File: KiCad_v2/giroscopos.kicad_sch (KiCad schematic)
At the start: 15 parts, among them U8 BNO085, U9 MPU-6050

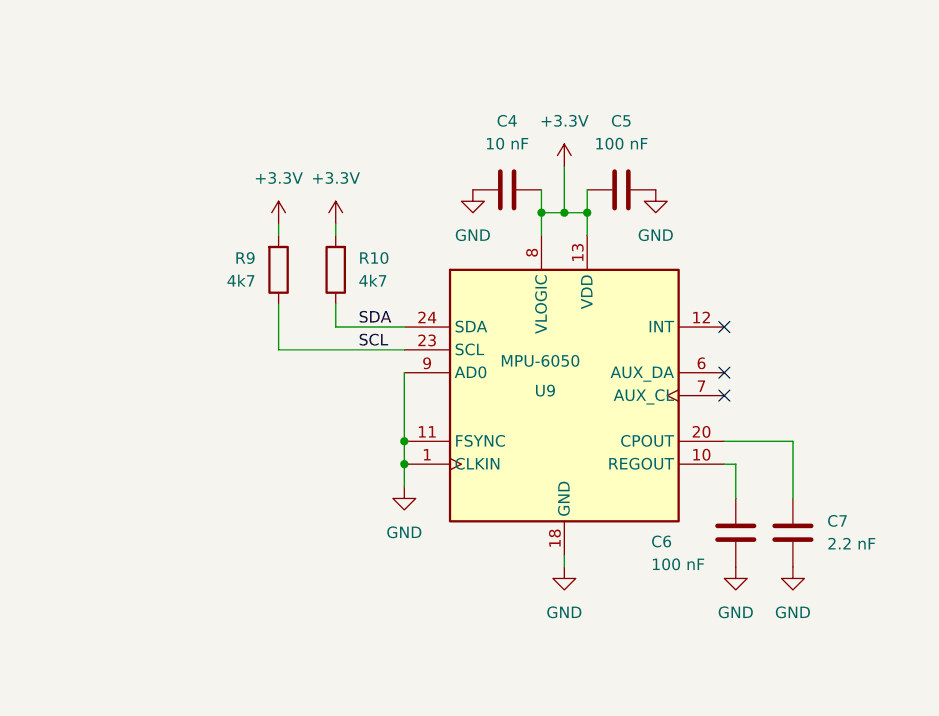
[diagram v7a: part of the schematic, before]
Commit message: feat: sigue rooteo y correccion de valores de resistencias
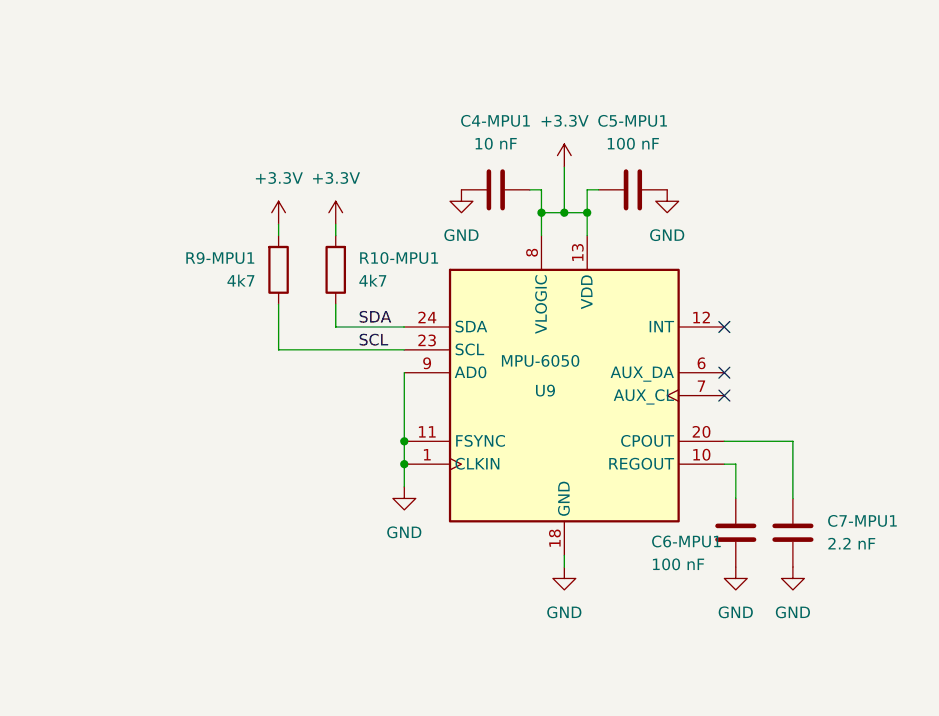
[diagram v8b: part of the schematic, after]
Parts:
- renumbered C4 to C4-MPU1, C5 to C5-MPU1, C6 to C6-MPU1, C7 to C7-MPU1, R10 to R10-MPU1, R9 to R9-MPU1
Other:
- moved on the sheet: C4-MPU1, C5-MPU1
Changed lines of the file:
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@@
 	(wire
 		(pts
+			(xy 227.33 68.58) (xy 228.6 68.58)
+		)
+		(stroke
+			(width 0)
+			(type default)
+		)
+	)
+	(wire
+		(pts
 			(xy 120.65 73.66) (xy 127 73.66)
 		)
@@
 	(wire
 		(pts
+			(xy 222.25 68.58) (xy 220.98 68.58)
+		)
+		(stroke
+			(width 0)
+			(type default)
+		)
+	)
+	(wire
+		(pts
 			(xy 214.63 148.59) (xy 228.6 148.59)
 		)
@@
 		(dnp no)
 		(fields_autoplaced yes)
-		(property "Reference" "C7"
+		(property "Reference" "C7-MPU1"
 			(at 254 105.4099 0)
 			(effects
@@
 			(project "SignaLink"
 				(path "/a1f5fcc2-f8ff-418d-9afd-dd6d7b5c6dc3/8a7116bd-bd79-4b86-b409-f716f8575102"
-					(reference "C7")
+					(reference "C7-MPU1")
 					(unit 1)
 				)
@@
 		(dnp no)
 		(fields_autoplaced yes)
-		(property "Reference" "R10"
+		(property "Reference" "R10-MPU1"
 			(at 201.93 76.1999 0)
 			(effects
@@
 			(project "SignaLink"
 				(path "/a1f5fcc2-f8ff-418d-9afd-dd6d7b5c6dc3/8a7116bd-bd79-4b86-b409-f716f8575102"
-					(reference "R10")
+					(reference "R10-MPU1")
 					(unit 1)
 				)
@@
 	(symbol
 		(lib_id "Device:C")
-		(at 231.14 68.58 90)
+		(at 232.41 68.58 90)
 		(unit 1)
 		(exclude_from_sim no)
@@
 		(on_board yes)
 		(dnp no)
-		(property "Reference" "C5"
-			(at 231.14 60.96 90)
+		(property "Reference" "C5-MPU1"
+			(at 232.41 60.96 90)
 			(effects
 				(font
@@
 		)
 		(property "Value" "100 nF"
-			(at 231.14 63.5 90)
+			(at 232.41 63.5 90)
 			(effects
 				(font
@@
 		)
 		(property "Footprint" "Capacitor_SMD:C_0603_1608Metric"
-			(at 234.95 67.6148 0)
+			(at 236.22 67.6148 0)
 			(effects
 				(font
@@
 		)
 		(property "Datasheet" "~"
-			(at 231.14 68.58 0)
+			(at 232.41 68.58 0)
 			(effects
 				(font
@@
 		)
 		(property "Description" "Unpolarized capacitor"
-			(at 231.14 68.58 0)
+			(at 232.41 68.58 0)
 			(effects
 				(font
@@
 		)
 		(property "Sim.Device" ""
-			(at 231.14 68.58 90)
+			(at 232.41 68.58 90)
 			(effects
 				(font
@@
 		)
 		(property "AVAILABILITY" ""
-			(at 231.14 68.58 90)
+			(at 232.41 68.58 90)
 			(effects
 				(font
@@
 		)
 		(property "DESCRIPTION" ""
-			(at 231.14 68.58 90)
+			(at 232.41 68.58 90)
 			(effects
 				(font
@@
 		)
 		(property "MANUFACTURER_PART_NUMBER" ""
-			(at 231.14 68.58 90)
+			(at 232.41 68.58 90)
 			(effects
 				(font
@@
 		)
 		(property "PACKAGE" ""
-			(at 231.14 68.58 90)
+			(at 232.41 68.58 90)
 			(effects
 				(font
@@
 		)
 		(property "PRICE" ""
-			(at 231.14 68.58 90)
+			(at 232.41 68.58 90)
 			(effects
 				(font
@@
 		)
 		(property "SNAPEDA_PACKAGE_ID" ""
-			(at 231.14 68.58 90)
+			(at 232.41 68.58 90)
 			(effects
 				(font
@@
 		)
 		(property "VENDOR" ""
-			(at 231.14 68.58 90)
+			(at 232.41 68.58 90)
 			(effects
 				(font
@@
 		)
 		(property "VALUE" ""
-			(at 231.14 68.58 90)
+			(at 232.41 68.58 90)
 			(effects
 				(font
@@
 			(project "SignaLink"
 				(path "/a1f5fcc2-f8ff-418d-9afd-dd6d7b5c6dc3/8a7116bd-bd79-4b86-b409-f716f8575102"
-					(reference "C5")
+					(reference "C5-MPU1")
 					(unit 1)
 				)
@@
 		(on_board yes)
 		(dnp no)
-		(property "Reference" "R9"
+		(property "Reference" "R9-MPU1"
 			(at 190.5 76.1999 0)
 			(effects
@@
 			(project "SignaLink"
 				(path "/a1f5fcc2-f8ff-418d-9afd-dd6d7b5c6dc3/8a7116bd-bd79-4b86-b409-f716f8575102"
-					(reference "R9")
+					(reference "R9-MPU1")
 					(unit 1)
 				)
@@
 		(on_board yes)
 		(dnp no)
-		(property "Reference" "C6"
+		(property "Reference" "C6-MPU1"
 			(at 234.442 107.696 0)
 			(effects
@@
 			(project "SignaLink"
 				(path "/a1f5fcc2-f8ff-418d-9afd-dd6d7b5c6dc3/8a7116bd-bd79-4b86-b409-f716f8575102"
-					(reference "C6")
+					(reference "C6-MPU1")
 					(unit 1)
 				)
@@
 	(symbol
 		(lib_id "power:GND")
-		(at 214.63 68.58 0)
+		(at 213.36 68.58 0)
 		(unit 1)
 		(exclude_from_sim no)
@@
 		(fields_autoplaced yes)
 		(property "Reference" "#PWR054"
-			(at 214.63 74.93 0)
+			(at 213.36 74.93 0)
 			(effects
 				(font
@@
 		)
 		(property "Value" "GND"
-			(at 214.63 73.66 0)
+			(at 213.36 73.66 0)
 			(effects
 				(font
@@
 		)
 		(property "Footprint" ""
-			(at 214.63 68.58 0)
+			(at 213.36 68.58 0)
 			(effects
 				(font
@@
 		)
 		(property "Datasheet" ""
-			(at 214.63 68.58 0)
+			(at 213.36 68.58 0)
 			(effects
 				(font
@@
 		)
 		(property "Description" "Power symbol creates a global label with name \"GND\" , ground"
-			(at 214.63 68.58 0)
+			(at 213.36 68.58 0)
 			(effects
 				(font
@@
 	(symbol
 		(lib_id "power:GND")
-		(at 234.95 68.58 0)
+		(at 236.22 68.58 0)
 		(unit 1)
 		(exclude_from_sim no)
@@
 		(fields_autoplaced yes)
 		(property "Reference" "#PWR057"
-			(at 234.95 74.93 0)
+			(at 236.22 74.93 0)
 			(effects
 				(font
@@
 		)
 		(property "Value" "GND"
-			(at 234.95 73.66 0)
+			(at 236.22 73.66 0)
 			(effects
 				(font
@@
 		)
 		(property "Footprint" ""
-			(at 234.95 68.58 0)
+			(at 236.22 68.58 0)
 			(effects
 				(font
@@
 		)
 		(property "Datasheet" ""
-			(at 234.95 68.58 0)
+			(at 236.22 68.58 0)
 			(effects
 				(font
@@
 		)
 		(property "Description" "Power symbol creates a global label with name \"GND\" , ground"
-			(at 234.95 68.58 0)
+			(at 236.22 68.58 0)
 			(effects
 				(font
@@
 	(symbol
 		(lib_id "Device:C")
-		(at 218.44 68.58 90)
+		(at 217.17 68.58 90)
 		(unit 1)
 		(exclude_from_sim no)
@@
 		(on_board yes)
 		(dnp no)
-		(property "Reference" "C4"
-			(at 218.44 60.96 90)
+		(property "Reference" "C4-MPU1"
+			(at 217.17 60.96 90)
 			(effects
 				(font
@@
 		)
 		(property "Value" "10 nF"
-			(at 218.44 63.5 90)
+			(at 217.17 63.5 90)
 			(effects
 				(font
@@
 		)
 		(property "Footprint" "Capacitor_SMD:C_0603_1608Metric"
-			(at 222.25 67.6148 0)
+			(at 220.98 67.6148 0)
 			(effects
 				(font
@@
 		)
 		(property "Datasheet" "~"
-			(at 218.44 68.58 0)
+			(at 217.17 68.58 0)
 			(effects
 				(font
@@
 		)
 		(property "Description" "Unpolarized capacitor"
-			(at 218.44 68.58 0)
+			(at 217.17 68.58 0)
 			(effects
 				(font
@@
 		)
 		(property "Sim.Device" ""
-			(at 218.44 68.58 90)
+			(at 217.17 68.58 90)
 			(effects
 				(font
@@
 		)
 		(property "AVAILABILITY" ""
-			(at 218.44 68.58 90)
+			(at 217.17 68.58 90)
 			(effects
 				(font
@@
 		)
 		(property "DESCRIPTION" ""
-			(at 218.44 68.58 90)
+			(at 217.17 68.58 90)
 			(effects
 				(font
@@
 		)
 		(property "MANUFACTURER_PART_NUMBER" ""
-			(at 218.44 68.58 90)
+			(at 217.17 68.58 90)
 			(effects
 				(font
@@
 		)
 		(property "PACKAGE" ""
-			(at 218.44 68.58 90)
+			(at 217.17 68.58 90)
 			(effects
 				(font
@@
 		)
 		(property "PRICE" ""
-			(at 218.44 68.58 90)
+			(at 217.17 68.58 90)
 			(effects
 				(font
@@
 		)
 		(property "SNAPEDA_PACKAGE_ID" ""
-			(at 218.44 68.58 90)
+			(at 217.17 68.58 90)
 			(effects
 				(font
@@
 		)
 		(property "VENDOR" ""
-			(at 218.44 68.58 90)
+			(at 217.17 68.58 90)
 			(effects
 				(font
@@
 		)
 		(property "VALUE" ""
-			(at 218.44 68.58 90)
+			(at 217.17 68.58 90)
 			(effects
 				(font
@@
 			(project "SignaLink"
 				(path "/a1f5fcc2-f8ff-418d-9afd-dd6d7b5c6dc3/8a7116bd-bd79-4b86-b409-f716f8575102"
-					(reference "C4")
+					(reference "C4-MPU1")
 					(unit 1)
 				)
